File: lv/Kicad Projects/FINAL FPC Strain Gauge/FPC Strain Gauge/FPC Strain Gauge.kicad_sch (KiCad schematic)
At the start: 0 parts

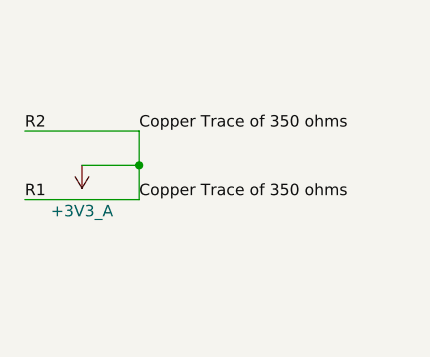
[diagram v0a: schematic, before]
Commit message: Finish Kicad Strain Gauge Design and Create a readme explaining it all
Finished FPC Strain Gauge
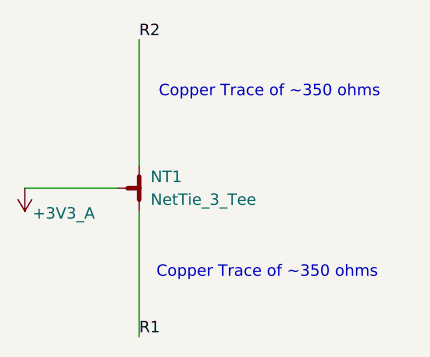
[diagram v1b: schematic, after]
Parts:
- added NT1: NetTie_3_Tee, NetTie:NetTie-3_SMD_Pad0.5mm, symbol Device:NetTie_3_Tee
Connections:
- net +3V3_A: now also NT1.3
- new net R1: NT1.2
- new net R2: NT1.1
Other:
- note added: "Copper Trace of ~350 ohms"
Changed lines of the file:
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@@
 		(comment 3 "${COMMENT2}")
 	)
-	(junction
-		(at 54.61 35.56)
-		(diameter 0)
-		(color 0 0 0 0)
+	(text "Copper Trace of ~350 ohms"
+		(exclude_from_sim no)
+		(at 68.834 47.498 0)
+		(effects
+			(font
+				(size 1.27 1.27)
+			)
+		)
+	)
+	(text "Copper Trace of ~350 ohms"
+		(exclude_from_sim no)
+		(at 69.088 27.432 0)
+		(effects
+			(font
+				(size 1.27 1.27)
+			)
+		)
 	)
 	(wire
 		(pts
-			(xy 54.61 35.56) (xy 54.61 31.75)
+			(xy 54.61 21.59) (xy 54.61 35.56)
 		)
 		(stroke
@@
 	(wire
 		(pts
-			(xy 54.61 35.56) (xy 54.61 39.37)
+			(xy 41.91 38.1) (xy 52.07 38.1)
 		)
 		(stroke
@@
 	(wire
 		(pts
-			(xy 48.26 35.56) (xy 54.61 35.56)
+			(xy 54.61 40.64) (xy 54.61 54.61)
 		)
 		(stroke
@@
 		)
 	)
-	(wire
-		(pts
-			(xy 41.91 31.75) (xy 54.61 31.75)
-		)
-		(stroke
-			(width 0)
-			(type default)
-		)
-	)
-	(wire
-		(pts
-			(xy 54.61 39.37) (xy 41.91 39.37)
-		)
-		(stroke
-			(width 0)
-			(type default)
-		)
-	)
 	(label "R1"
-		(at 41.91 39.37 0)
+		(at 54.61 54.61 0)
 		(effects
 			(font
@@
 		)
 	)
-	(label "Copper Trace of 350 ohms"
-		(at 54.61 39.37 0)
-		(effects
-			(font
-				(size 1.27 1.27)
-			)
-			(justify left bottom)
-		)
-	)
 	(label "R2"
-		(at 41.91 31.75 0)
-		(effects
-			(font
-				(size 1.27 1.27)
-			)
-			(justify left bottom)
-		)
-	)
-	(label "Copper Trace of 350 ohms"
-		(at 54.61 31.75 0)
+		(at 54.61 21.59 0)
 		(effects
 			(font
@@
 	(symbol
 		(lib_id "power:+3.3VA")
-		(at 48.26 35.56 0)
+		(at 41.91 38.1 0)
 		(mirror x)
 		(unit 1)
@@
 		(dnp no)
 		(property "Reference" "#PWR01"
-			(at 48.26 31.75 0)
+			(at 41.91 34.29 0)
 			(hide yes)
 			(show_name no)
@@
 		)
 		(property "Value" "+3V3_A"
-			(at 48.26 40.64 0)
+			(at 46.228 40.894 0)
 			(show_name no)
 			(do_not_autoplace no)
@@
 		)
 		(property "Footprint" ""
-			(at 48.26 35.56 0)
+			(at 41.91 38.1 0)
 			(hide yes)
 			(show_name no)
@@
 		)
 		(property "Datasheet" ""
-			(at 48.26 35.56 0)
+			(at 41.91 38.1 0)
 			(hide yes)
 			(show_name no)
@@
 		)
 		(property "Description" "Power symbol creates a global label with name \"+3.3VA\""
-			(at 48.26 35.56 0)
+			(at 41.91 38.1 0)
 			(hide yes)
 			(show_name no)
@@
 					(unit 1)
 				)
+			)
+		)
+	)
+	(symbol
+		(lib_id "Device:NetTie_3_Tee")
+		(at 54.61 38.1 270)
+		(unit 1)
+		(body_style 1)
+		(exclude_from_sim no)
+		(in_bom no)
+		(on_board yes)
+		(in_pos_files yes)
+		(dnp no)
+		(fields_autoplaced yes)
+		(property "Reference" "NT1"
+			(at 55.88 36.8299 90)
+			(show_name no)
+			(do_not_autoplace no)
+			(effects
+				(font
+					(size 1.27 1.27)
+				)
+				(justify left)
+			)
+		)
+		(property "Value" "NetTie_3_Tee"
+			(at 55.88 39.3699 90)
+			(show_name no)
+			(do_not_autoplace no)
+			(effects
+				(font
+					(size 1.27 1.27)
+				)
+				(justify left)
+			)
+		)
+		(property "Footprint" "NetTie:NetTie-3_SMD_Pad0.5mm"
+			(at 54.61 38.1 0)
+			(hide yes)
+			(show_name no)
+			(do_not_autoplace no)
+			(effects
+				(font
+					(size 1.27 1.27)
+				)
+			)
+		)
+		(property "Datasheet" ""
+			(at 54.61 38.1 0)
+			(hide yes)
+			(show_name no)
+			(do_not_autoplace no)
+			(effects
+				(font
+					(size 1.27 1.27)
+				)
+			)
+		)
+		(property "Description" "Net tie, 3 pins, tee"
+			(at 54.61 38.1 0)
+			(hide yes)
+			(show_name no)
+			(do_not_autoplace no)
+			(effects
+				(font
+					(size 1.27 1.27)
+				)
+			)
+		)
+		(pin "2"
+		)
+		(pin "1"
+		)
+		(pin "3"
+		)
+		(instances
+			(project "FPC Strain Gauge"
+				(path "/e994741c-7c7d-4124-9d00-43b883baa61d"
+					(reference "NT1")
+					(unit 1)
+				)
